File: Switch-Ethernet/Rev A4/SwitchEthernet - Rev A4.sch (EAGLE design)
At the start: 111 parts, among them J1 22-05-7028-02, J2 DF17(2.0)-20DP-0.5V(57), J3 DF17(4.0)-20DP-0.5V(57), J4 22-05-7058-05, P1 RB1-125BAG1A, T1 H1102FNL, T2 H1102FNL, U1 TC1264-3.3, U2 TC1264-1.8, U3 KSZ8995MA, U4 AT24C02C-SSHM-B, X1 NE8FAV, X2 NE8FAV, Y1 8Z-25.000MHZMAAJ-T

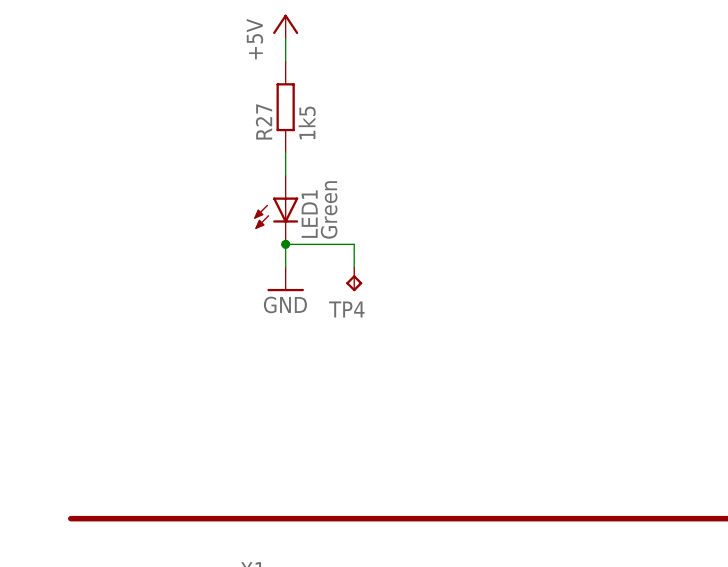
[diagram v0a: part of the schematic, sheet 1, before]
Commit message: Route LED +5V
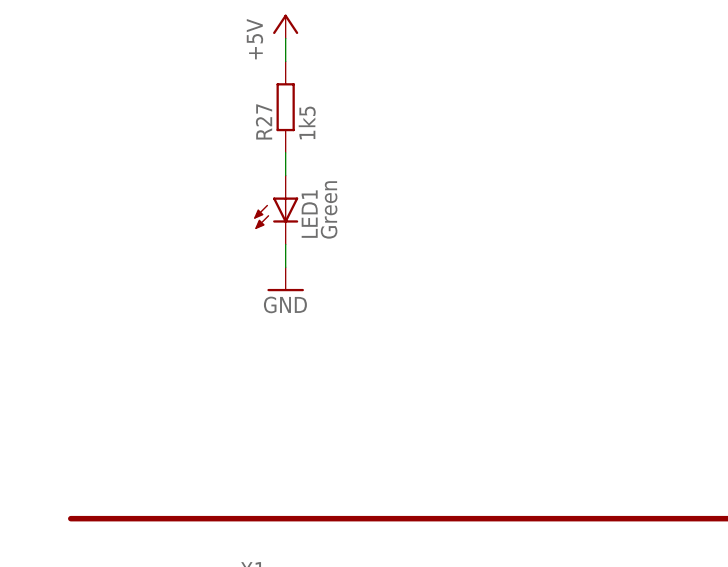
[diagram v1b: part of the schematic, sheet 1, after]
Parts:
- removed TP4: TPB1,27, testpad:TPB1,27
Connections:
- net GND: no longer TP4.TP
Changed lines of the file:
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@@
 <part name="+1V10" library="supply1" deviceset="+1V8" device=""/>
 <part name="+1V11" library="supply1" deviceset="+1V8" device=""/>
-<part name="TP4" library="testpad" deviceset="TP" device="B1,27">
-<attribute name="MF" value=""/>
-<attribute name="MPN" value=""/>
-<attribute name="OC_FARNELL" value="unknown"/>
-<attribute name="OC_NEWARK" value="unknown"/>
-</part>
 <part name="LED4" library="led" deviceset="LED" device="CHIP-LED0603" value="Blue">
 <attribute name="MF" value="MULTICOMP"/>
@@
 <instance part="GND15" gate="1" x="27.94" y="165.1"/>
 <instance part="P+3" gate="1" x="27.94" y="195.58"/>
-<instance part="TP4" gate="G$1" x="35.56" y="165.1" rot="R180">
-<attribute name="OC_NEWARK" x="35.56" y="165.1" size="1.778" layer="96" display="off"/>
-<attribute name="MF" x="35.56" y="165.1" size="1.778" layer="96" display="off"/>
-<attribute name="MPN" x="35.56" y="165.1" size="1.778" layer="96" display="off"/>
-<attribute name="OC_FARNELL" x="35.56" y="165.1" size="1.778" layer="96" display="off"/>
-</instance>
 <instance part="LED4" gate="G$1" x="88.9" y="99.06">
 <attribute name="OC_NEWARK" x="88.9" y="99.06" size="1.778" layer="96" display="off"/>
@@
 </segment>
 <segment>
+<pinref part="LED1" gate="G$1" pin="C"/>
 <pinref part="GND15" gate="1" pin="GND"/>
-<pinref part="LED1" gate="G$1" pin="C"/>
 <wire x1="27.94" y1="167.64" x2="27.94" y2="170.18" width="0.1524" layer="91"/>
-<pinref part="TP4" gate="G$1" pin="TP"/>
-<wire x1="27.94" y1="170.18" x2="35.56" y2="170.18" width="0.1524" layer="91"/>
-<wire x1="35.56" y1="170.18" x2="35.56" y2="167.64" width="0.1524" layer="91"/>
-<junction x="27.94" y="170.18"/>
-</segment>
-<segment>
+</segment>
+<segment>

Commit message: Finish the routing
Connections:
- net GND: no longer J2-11.P, J2-14.P, J2-17.P, J2-4.P, J2-7.P, J3-11.P, J3-14.P, J3-17.P, J3-4.P, J3-7.P
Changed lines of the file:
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@@
 <attribute name="OC_FARNELL" value="unknown"/>
 </part>
-<part name="GND34" library="supply1" deviceset="GND" device=""/>
 <part name="+3V12" library="supply1" deviceset="+3V3" device=""/>
-<part name="GND35" library="supply1" deviceset="GND" device=""/>
 <part name="+3V16" library="supply1" deviceset="+3V3" device=""/>
 <part name="J2" library="con-hirose" deviceset="DF17(?)-20DP-0.5V(57)" device="2.0"/>
@@
 <instance part="+3V10" gate="G$1" x="88.9" y="121.92" rot="MR0"/>
 <instance part="+3V11" gate="G$1" x="88.9" y="60.96" rot="MR0"/>
-<instance part="GND34" gate="1" x="116.84" y="45.72" rot="MR0"/>
 <instance part="+3V12" gate="G$1" x="116.84" y="116.84" rot="MR0"/>
-<instance part="GND35" gate="1" x="190.5" y="45.72"/>
 <instance part="+3V16" gate="G$1" x="190.5" y="116.84"/>
 <instance part="J2" gate="-1" x="139.7" y="104.14"/>
@@
 <wire x1="205.74" y1="162.56" x2="205.74" y2="167.64" width="0.1524" layer="91"/>
 </segment>
-<segment>
-<wire x1="134.62" y1="88.9" x2="116.84" y2="88.9" width="0.1524" layer="91"/>
-<wire x1="116.84" y1="88.9" x2="116.84" y2="71.12" width="0.1524" layer="91"/>
-<pinref part="GND34" gate="1" pin="GND"/>
-<wire x1="116.84" y1="71.12" x2="116.84" y2="63.5" width="0.1524" layer="91"/>
-<wire x1="116.84" y1="63.5" x2="116.84" y2="55.88" width="0.1524" layer="91"/>
-<wire x1="116.84" y1="55.88" x2="116.84" y2="48.26" width="0.1524" layer="91"/>
-<wire x1="134.62" y1="55.88" x2="116.84" y2="55.88" width="0.1524" layer="91"/>
-<junction x="116.84" y="55.88"/>
-<wire x1="134.62" y1="63.5" x2="116.84" y2="63.5" width="0.1524" layer="91"/>
-<junction x="116.84" y="63.5"/>
-<wire x1="134.62" y1="71.12" x2="116.84" y2="71.12" width="0.1524" layer="91"/>
-<junction x="116.84" y="71.12"/>
-<wire x1="134.62" y1="96.52" x2="116.84" y2="96.52" width="0.1524" layer="91"/>
-<wire x1="116.84" y1="96.52" x2="116.84" y2="88.9" width="0.1524" layer="91"/>
-<junction x="116.84" y="88.9"/>
-<pinref part="J2" gate="-4" pin="P"/>
-<pinref part="J2" gate="-7" pin="P"/>
-<pinref part="J2" gate="-17" pin="P"/>
-<pinref part="J2" gate="-14" pin="P"/>
-<pinref part="J2" gate="-11" pin="P"/>
-</segment>
-<segment>
-<wire x1="172.72" y1="88.9" x2="190.5" y2="88.9" width="0.1524" layer="91"/>
-<wire x1="190.5" y1="88.9" x2="190.5" y2="71.12" width="0.1524" layer="91"/>
-<pinref part="GND35" gate="1" pin="GND"/>
-<wire x1="190.5" y1="71.12" x2="190.5" y2="63.5" width="0.1524" layer="91"/>
-<wire x1="190.5" y1="63.5" x2="190.5" y2="55.88" width="0.1524" layer="91"/>
-<wire x1="190.5" y1="55.88" x2="190.5" y2="48.26" width="0.1524" layer="91"/>
-<wire x1="172.72" y1="55.88" x2="190.5" y2="55.88" width="0.1524" layer="91"/>
-<junction x="190.5" y="55.88"/>
-<wire x1="172.72" y1="63.5" x2="190.5" y2="63.5" width="0.1524" layer="91"/>
-<junction x="190.5" y="63.5"/>
-<wire x1="172.72" y1="71.12" x2="190.5" y2="71.12" width="0.1524" layer="91"/>
-<junction x="190.5" y="71.12"/>
-<wire x1="172.72" y1="96.52" x2="190.5" y2="96.52" width="0.1524" layer="91"/>
-<wire x1="190.5" y1="96.52" x2="190.5" y2="88.9" width="0.1524" layer="91"/>
-<junction x="190.5" y="88.9"/>
-<pinref part="J3" gate="-4" pin="P"/>
-<pinref part="J3" gate="-7" pin="P"/>
-<pinref part="J3" gate="-17" pin="P"/>
-<pinref part="J3" gate="-14" pin="P"/>
-<pinref part="J3" gate="-11" pin="P"/>
-</segment>
 </net>

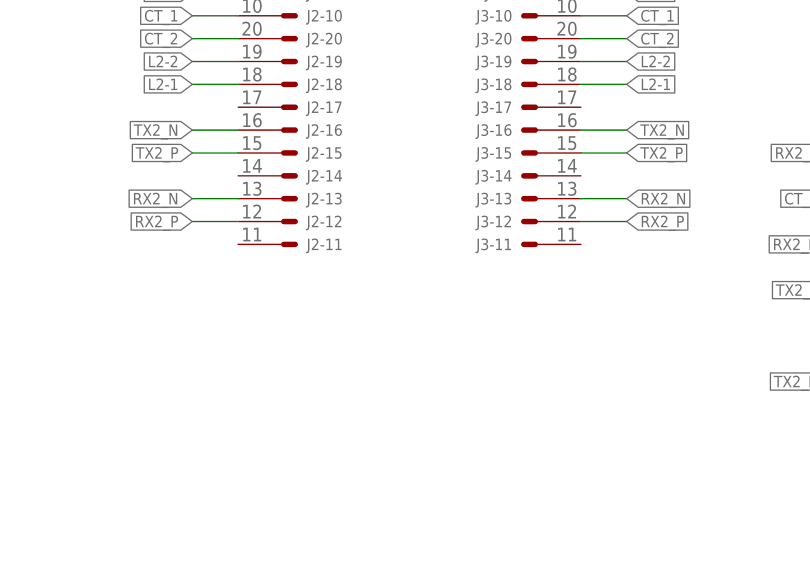
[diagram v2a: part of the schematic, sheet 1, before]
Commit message: Add bRestrict on the Neutrix panel and route GND nets
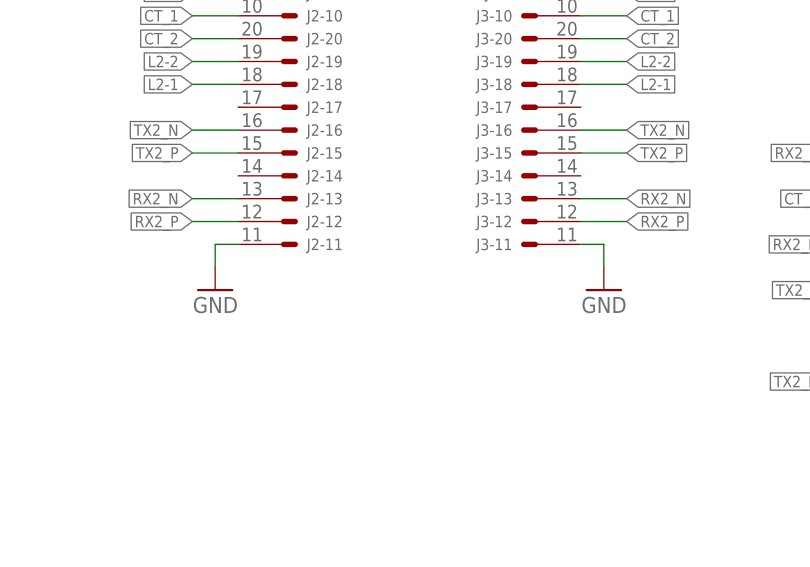
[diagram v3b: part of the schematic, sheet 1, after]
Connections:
- net GND: now also J2-11.P, J3-11.P
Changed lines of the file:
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@@
 <part name="J3" library="con-hirose" deviceset="DF17(?)-20DP-0.5V(57)" device="4.0"/>
 <part name="J4" library="con-molex" deviceset="22-?-05" device="05-7058"/>
+<part name="GND30" library="supply1" deviceset="GND" device=""/>
+<part name="GND31" library="supply1" deviceset="GND" device=""/>
 </parts>
 <sheets>
@@
 <instance part="J3" gate="-12" x="167.64" y="58.42" rot="MR0"/>
 <instance part="J3" gate="-11" x="167.64" y="55.88" rot="MR0"/>
+<instance part="GND30" gate="1" x="132.08" y="50.8" rot="MR0"/>
+<instance part="GND31" gate="1" x="175.26" y="50.8" rot="MR0"/>
 </instances>
 <busses>
@@
 <wire x1="205.74" y1="162.56" x2="205.74" y2="167.64" width="0.1524" layer="91"/>
 </segment>
+<segment>
+<pinref part="GND30" gate="1" pin="GND"/>
+<pinref part="J2" gate="-11" pin="P"/>
+<wire x1="132.08" y1="53.34" x2="132.08" y2="55.88" width="0.1524" layer="91"/>
+<wire x1="132.08" y1="55.88" x2="134.62" y2="55.88" width="0.1524" layer="91"/>
+</segment>
+<segment>
+<pinref part="J3" gate="-11" pin="P"/>
+<pinref part="GND31" gate="1" pin="GND"/>
+<wire x1="172.72" y1="55.88" x2="175.26" y2="55.88" width="0.1524" layer="91"/>
+<wire x1="175.26" y1="55.88" x2="175.26" y2="53.34" width="0.1524" layer="91"/>
+</segment>
 </net>

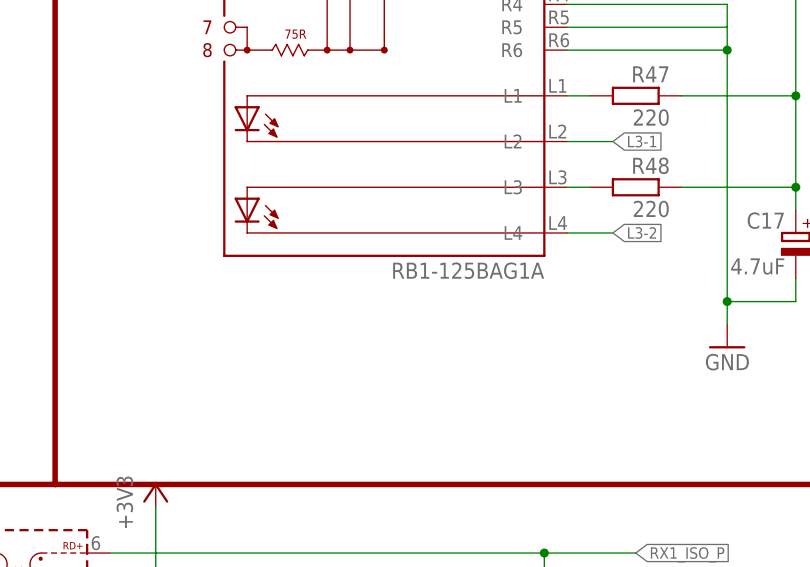
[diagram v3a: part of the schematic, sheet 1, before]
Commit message: Add via to the guard ring
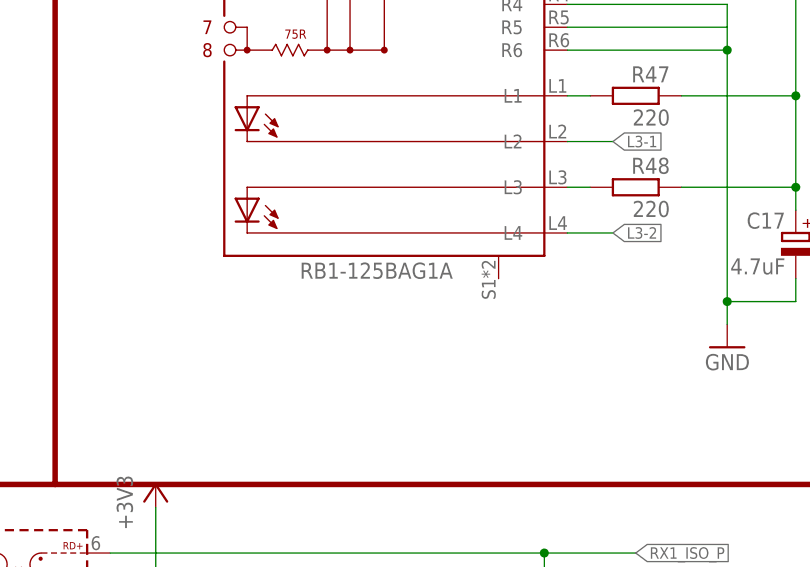
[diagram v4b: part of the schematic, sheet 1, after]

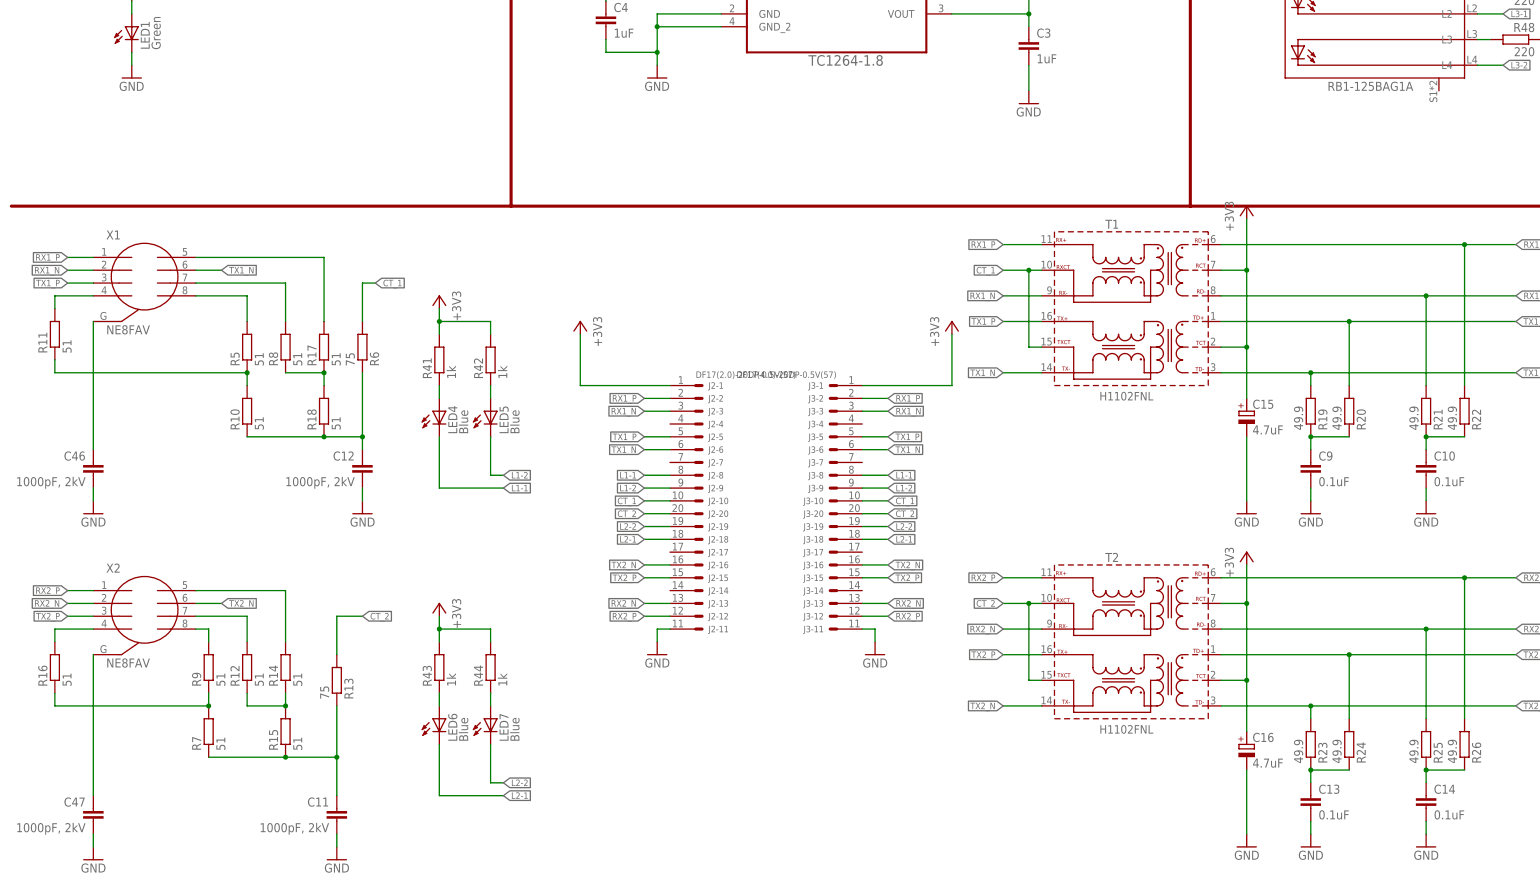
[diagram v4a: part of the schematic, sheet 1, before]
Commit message: Connect GND meca of the connectors to the guard ring
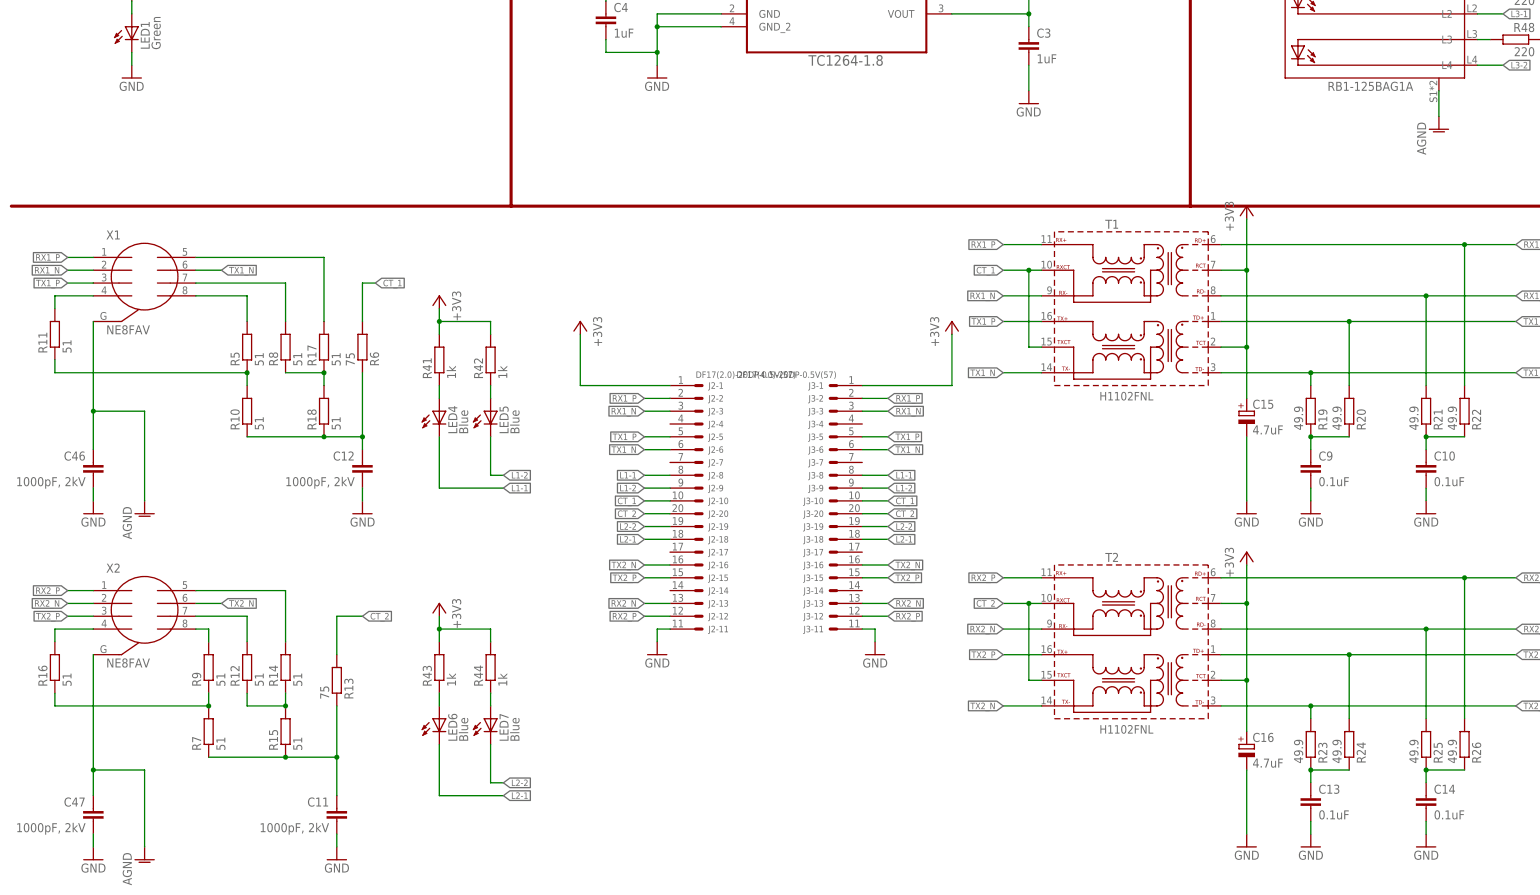
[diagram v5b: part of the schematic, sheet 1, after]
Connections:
- removed net N$36: C47.1, X2.G
- removed net N$37: C46.1, X1.G
- new net AGND: C46.1, C47.1, P1.P$1, X1.G, X2.G
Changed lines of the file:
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@@
 <part name="GND30" library="supply1" deviceset="GND" device=""/>
 <part name="GND31" library="supply1" deviceset="GND" device=""/>
+<part name="AGND1" library="supply1" deviceset="AGND" device=""/>
+<part name="AGND2" library="supply1" deviceset="AGND" device=""/>
+<part name="AGND3" library="supply1" deviceset="AGND" device=""/>
 </parts>
 <sheets>
@@
 <instance part="GND30" gate="1" x="132.08" y="50.8" rot="MR0"/>
 <instance part="GND31" gate="1" x="175.26" y="50.8" rot="MR0"/>
+<instance part="AGND1" gate="VR1" x="30.48" y="10.16"/>
+<instance part="AGND2" gate="VR1" x="30.48" y="78.74"/>
+<instance part="AGND3" gate="VR1" x="287.02" y="154.94"/>
 </instances>
 <busses>
@@
 </segment>
 </net>
-<net name="N$36" class="0">
-<segment>
-<pinref part="C47" gate="G$1" pin="1"/>
-<pinref part="X2" gate="G$1" pin="G"/>
-<wire x1="20.32" y1="22.86" x2="20.32" y2="50.8" width="0.1524" layer="91"/>
-</segment>
-</net>
-<net name="N$37" class="0">
-<segment>
-<pinref part="X1" gate="G$1" pin="G"/>
-<pinref part="C46" gate="G$1" pin="1"/>
-<wire x1="20.32" y1="116.84" x2="20.32" y2="91.44" width="0.1524" layer="91"/>
-</segment>
-</net>
 <net name="+1V8" class="0">
 <segment>
@@
 </segment>
 </net>
+<net name="AGND" class="0">
+<segment>
+<pinref part="AGND3" gate="VR1" pin="AGND"/>
+<pinref part="P1" gate="G$1" pin="P$1"/>
+<wire x1="287.02" y1="157.48" x2="287.02" y2="162.56" width="0.1524" layer="91"/>
+</segment>
+<segment>
+<pinref part="X1" gate="G$1" pin="G"/>
+<pinref part="C46" gate="G$1" pin="1"/>
+<wire x1="20.32" y1="116.84" x2="20.32" y2="99.06" width="0.1524" layer="91"/>
+<pinref part="AGND2" gate="VR1" pin="AGND"/>
+<wire x1="20.32" y1="99.06" x2="20.32" y2="91.44" width="0.1524" layer="91"/>
+<wire x1="30.48" y1="81.28" x2="30.48" y2="99.06" width="0.1524" layer="91"/>
+<wire x1="30.48" y1="99.06" x2="20.32" y2="99.06" width="0.1524" layer="91"/>
+<junction x="20.32" y="99.06"/>
+</segment>
+<segment>
+<pinref part="C47" gate="G$1" pin="1"/>
+<pinref part="X2" gate="G$1" pin="G"/>
+<wire x1="20.32" y1="22.86" x2="20.32" y2="27.94" width="0.1524" layer="91"/>
+<pinref part="AGND1" gate="VR1" pin="AGND"/>
+<wire x1="20.32" y1="27.94" x2="20.32" y2="50.8" width="0.1524" layer="91"/>
+<wire x1="30.48" y1="12.7" x2="30.48" y2="27.94" width="0.1524" layer="91"/>
+<wire x1="30.48" y1="27.94" x2="20.32" y2="27.94" width="0.1524" layer="91"/>
+<junction x="20.32" y="27.94"/>
+</segment>
+</net>

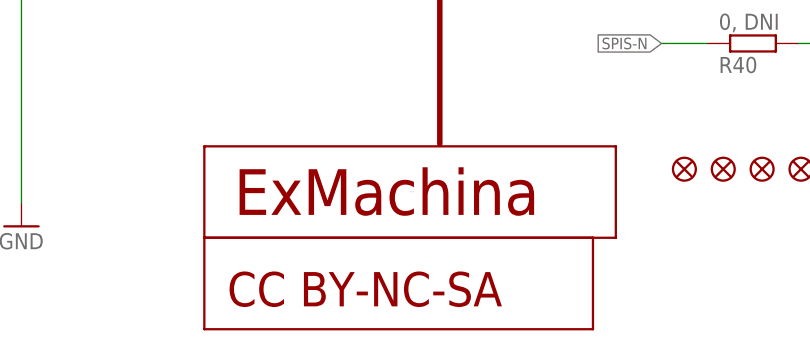
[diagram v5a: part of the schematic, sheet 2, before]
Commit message: Add the cotation, the board name, the logo and the CC
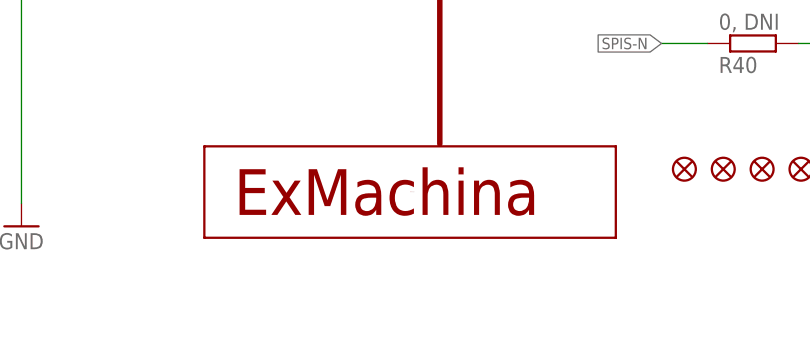
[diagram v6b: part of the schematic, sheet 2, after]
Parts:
- removed U$7: CC-BY-NC-SA, cc-by-sa:CC-BY-NC-SA
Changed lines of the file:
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@@
 <part name="+3V10" library="supply1" deviceset="+3V3" device=""/>
 <part name="+3V11" library="supply1" deviceset="+3V3" device=""/>
-<part name="U$7" library="cc-by-sa" deviceset="CC-BY-NC-SA" device="">
-<attribute name="MF" value=""/>
-<attribute name="MPN" value=""/>
-<attribute name="OC_FARNELL" value="unknown"/>
-</part>
 <part name="+3V12" library="supply1" deviceset="+3V3" device=""/>
 <part name="+3V16" library="supply1" deviceset="+3V3" device=""/>
@@
 <attribute name="MPN" x="358.394" y="21.59" size="1.778" layer="96" display="off"/>
 </instance>
-<instance part="U$7" gate="G$1" x="307.34" y="8.89">
-<attribute name="OC_FARNELL" x="307.34" y="8.89" size="1.778" layer="96" display="off"/>
-<attribute name="MF" x="307.34" y="8.89" size="1.778" layer="96" display="off"/>
-<attribute name="MPN" x="307.34" y="8.89" size="1.778" layer="96" display="off"/>
-</instance>
 <instance part="J4" gate="-1" x="368.3" y="119.38"/>
